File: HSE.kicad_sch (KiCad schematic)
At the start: 5 parts, among them Y1 25MHz

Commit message: BOM cleaned up.
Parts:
- C10, C11: Notes (none) -> or equivalent; Package (none) -> C_0603_1608Metric
- R30: Notes (none) -> or equivalent; Package (none) -> R_0603_1608Metric
- Y1: Notes (none) -> or equivalent; Package (none) -> Crystal_SMD_2016-4Pin_2.0x1.6mm
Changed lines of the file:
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@@
 			)
 		)
-		(property "Datasheet" "~"
+		(property "Datasheet" ""
 			(at 154.94 109.22 0)
 			(effects
@@
 		)
 		(property "MfgPart" "CL10C100JB8NNNC"
+			(at 154.94 109.22 0)
+			(effects
+				(font
+					(size 1.27 1.27)
+				)
+				(hide yes)
+			)
+		)
+		(property "Package" "C_0603_1608Metric"
+			(at 154.94 109.22 0)
+			(effects
+				(font
+					(size 1.27 1.27)
+				)
+				(hide yes)
+			)
+		)
+		(property "Notes" "or equivalent"
 			(at 154.94 109.22 0)
 			(effects
@@
 			)
 		)
-		(property "Datasheet" "~"
+		(property "Datasheet" ""
 			(at 154.94 82.55 0)
 			(effects
@@
 		)
 		(property "MfgPart" "RC0603FR-07634RL"
+			(at 154.94 82.55 0)
+			(effects
+				(font
+					(size 1.27 1.27)
+				)
+				(hide yes)
+			)
+		)
+		(property "Package" "R_0603_1608Metric"
+			(at 154.94 82.55 0)
+			(effects
+				(font
+					(size 1.27 1.27)
+				)
+				(hide yes)
+			)
+		)
+		(property "Notes" "or equivalent"
 			(at 154.94 82.55 0)
 			(effects
@@
 			)
 		)
-		(property "Datasheet" "~"
-			(at 147.32 93.98 0)
-			(effects
-				(font
-					(size 1.27 1.27)
-				)
-				(hide yes)
-			)
-		)
-		(property "Description" "Four pin crystal, GND on pins 2 and 4"
+		(property "Datasheet" "https://support.epson.biz/td/api/doc_check.php?dl=brief_FA-128&lang=en"
+			(at 147.32 93.98 0)
+			(effects
+				(font
+					(size 1.27 1.27)
+				)
+				(hide yes)
+			)
+		)
+		(property "Description" "Four pin crystal, GND on pins 2 and 4, 7pF"
 			(at 147.32 93.98 0)
 			(effects
@@
 		)
 		(property "pads" "4"
+			(at 147.32 93.98 0)
+			(effects
+				(font
+					(size 1.27 1.27)
+				)
+				(hide yes)
+			)
+		)
+		(property "Package" "Crystal_SMD_2016-4Pin_2.0x1.6mm"
+			(at 147.32 93.98 0)
+			(effects
+				(font
+					(size 1.27 1.27)
+				)
+				(hide yes)
+			)
+		)
+		(property "Notes" "or equivalent"
 			(at 147.32 93.98 0)
 			(effects
@@
 			)
 		)
+		(property "Package" ""
+			(at 128.27 123.19 0)
+			(effects
+				(font
+					(size 1.27 1.27)
+				)
+				(hide yes)
+			)
+		)
 		(pin "2"
 		)
@@
 			)
 		)
-		(property "Datasheet" "~"
+		(property "Datasheet" ""
 			(at 138.43 109.22 0)
 			(effects
@@
 			(at 138.43 109.22 0)
 			(effects
+				(font
+					(size 1.27 1.27)
+				)
+				(hide yes)
+			)
+		)
+		(property "Package" "C_0603_1608Metric"
+			(at 138.43 109.22 0)
+			(effects
+				(font
+					(size 1.27 1.27)
+				)
+				(hide yes)
+			)
+		)
+		(property "Notes" "or equivalent"
+			(at 138.43 109.22 0)
+			(effects

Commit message: converted R, C, and L to smaller 0402 footprints. Some trace rearranging and cleanup.
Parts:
- C10, C11: footprint ProjectLib:C_0603_1608Metric -> ProjectLib:C_0402_1005Metric; Manufacturer Samsung -> (none); MfgPart CL10C100JB8NNNC -> (none); Package C_0603_1608Metric -> C_0402_1005Metric
- R30: footprint ProjectLib:R_0603_1608Metric -> ProjectLib:R_0402_1005Metric; Manufacturer Yageo -> (none); MfgPart RC0603FR-07634RL -> (none); Package R_0603_1608Metric -> R_0402_1005Metric
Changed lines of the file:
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@@
 			)
 		)
-		(property "Footprint" "ProjectLib:C_0603_1608Metric"
+		(property "Footprint" "ProjectLib:C_0402_1005Metric"
 			(at 153.9748 105.41 0)
 			(effects
@@
 			)
 		)
-		(property "Manufacturer" "Samsung"
-			(at 154.94 109.22 0)
-			(effects
-				(font
-					(size 1.27 1.27)
-				)
-				(hide yes)
-			)
-		)
-		(property "MfgPart" "CL10C100JB8NNNC"
-			(at 154.94 109.22 0)
-			(effects
-				(font
-					(size 1.27 1.27)
-				)
-				(hide yes)
-			)
-		)
-		(property "Package" "C_0603_1608Metric"
+		(property "Manufacturer" ""
+			(at 154.94 109.22 0)
+			(effects
+				(font
+					(size 1.27 1.27)
+				)
+				(hide yes)
+			)
+		)
+		(property "MfgPart" ""
+			(at 154.94 109.22 0)
+			(effects
+				(font
+					(size 1.27 1.27)
+				)
+				(hide yes)
+			)
+		)
+		(property "Package" "C_0402_1005Metric"
 			(at 154.94 109.22 0)
 			(effects
@@
 			)
 		)
-		(property "Footprint" "ProjectLib:R_0603_1608Metric"
+		(property "Footprint" "ProjectLib:R_0402_1005Metric"
 			(at 155.956 82.804 90)
 			(effects
@@
 			)
 		)
-		(property "Manufacturer" "Yageo"
-			(at 154.94 82.55 0)
-			(effects
-				(font
-					(size 1.27 1.27)
-				)
-				(hide yes)
-			)
-		)
-		(property "MfgPart" "RC0603FR-07634RL"
-			(at 154.94 82.55 0)
-			(effects
-				(font
-					(size 1.27 1.27)
-				)
-				(hide yes)
-			)
-		)
-		(property "Package" "R_0603_1608Metric"
+		(property "Manufacturer" ""
+			(at 154.94 82.55 0)
+			(effects
+				(font
+					(size 1.27 1.27)
+				)
+				(hide yes)
+			)
+		)
+		(property "MfgPart" ""
+			(at 154.94 82.55 0)
+			(effects
+				(font
+					(size 1.27 1.27)
+				)
+				(hide yes)
+			)
+		)
+		(property "Package" "R_0402_1005Metric"
 			(at 154.94 82.55 0)
 			(effects
@@
 			)
 		)
-		(property "Footprint" "ProjectLib:C_0603_1608Metric"
+		(property "Footprint" "ProjectLib:C_0402_1005Metric"
 			(at 137.4648 105.41 0)
 			(effects
@@
 			)
 		)
-		(property "Manufacturer" "Samsung"
+		(property "Manufacturer" ""
 			(at 138.43 109.22 0)
 			(effects
@@
 			)
 		)
-		(property "MfgPart" "CL10C100JB8NNNC"
+		(property "MfgPart" ""
 			(at 138.43 109.22 0)
 			(effects
@@
 			)
 		)
-		(property "Package" "C_0603_1608Metric"
+		(property "Package" "C_0402_1005Metric"
 			(at 138.43 109.22 0)
 			(effects

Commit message: improved schematic sheet titles.
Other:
- title: ADCs for 10K thermistors -> HSE
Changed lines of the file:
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@@
 	(paper "A4")
 	(title_block
-		(title "ADCs for 10K thermistors")
-		(date "2025-01-07")
-		(rev "v0.1.1")
+		(title "HSE")
+		(date "2025-09-15")
+		(rev "v0.2.2")
 	)
 	(junction

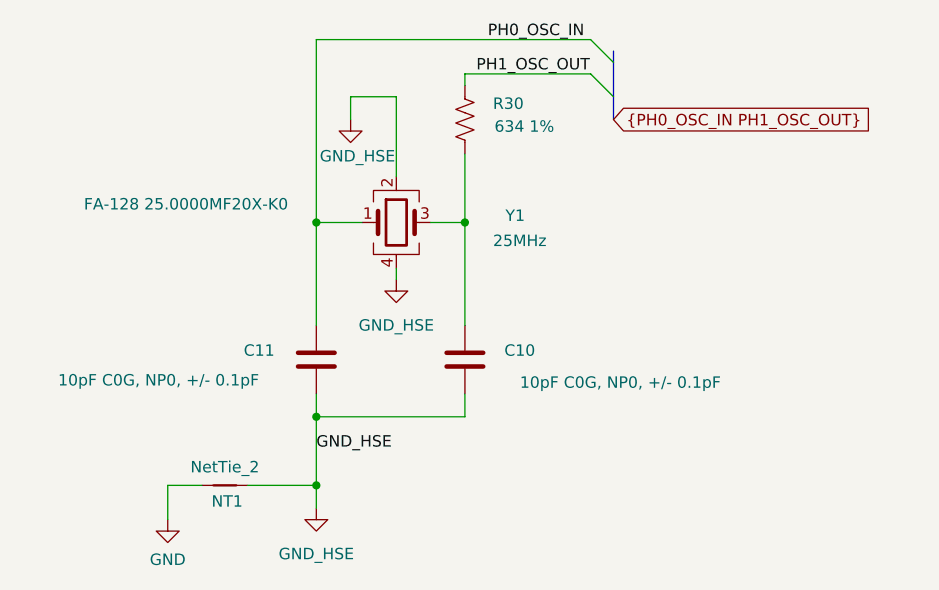
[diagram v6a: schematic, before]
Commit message: added QR and ID blocks on silkscreen. Marked HSE and LSE as DNP. Revised version number to 0.3.1.
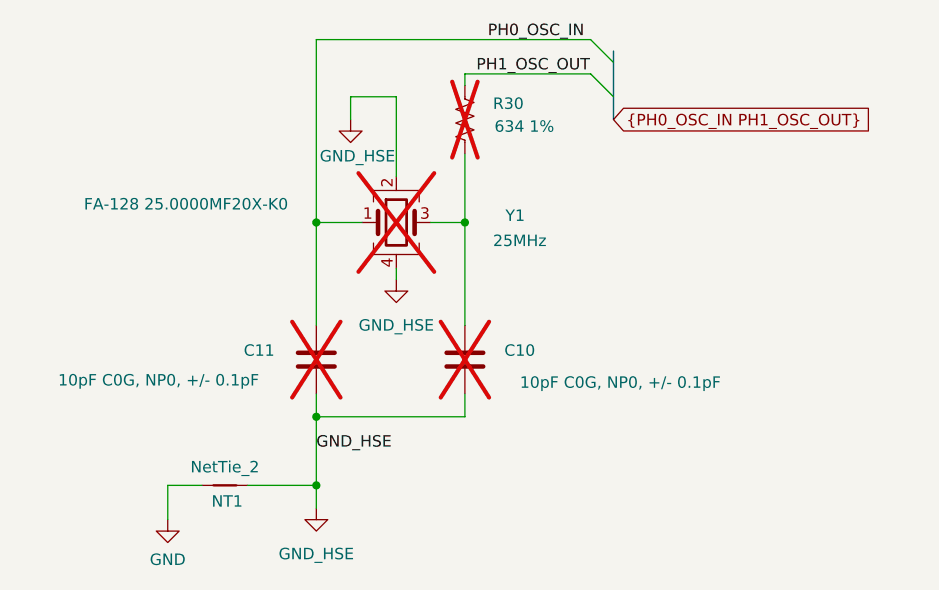
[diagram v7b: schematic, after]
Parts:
- C10, C11, R30, Y1: now not fitted
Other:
- title: HSE -> stm32f411, RFM95W
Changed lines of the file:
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@@
 	(paper "A4")
 	(title_block
-		(title "HSE")
-		(date "2025-09-15")
-		(rev "v0.2.2")
+		(title "stm32f411, RFM95W")
+		(date "2026-04-12")
+		(rev "v0.3.1")
 	)
 	(junction
@@
 		(in_bom yes)
 		(on_board yes)
-		(in_pos_files yes)
-		(dnp no)
+		(in_pos_files no)
+		(dnp yes)
 		(property "Reference" "C10"
 			(at 161.036 108.204 0)
@@
 		(in_bom yes)
 		(on_board yes)
-		(in_pos_files yes)
-		(dnp no)
+		(in_pos_files no)
+		(dnp yes)
 		(property "Reference" "R30"
 			(at 159.766 80.772 0)
@@
 		(in_bom yes)
 		(on_board yes)
-		(in_pos_files yes)
-		(dnp no)
+		(in_pos_files no)
+		(dnp yes)
 		(property "Reference" "Y1"
 			(at 160.528 93.218 0)
@@
 		(in_bom yes)
 		(on_board yes)
-		(in_pos_files yes)
-		(dnp no)
+		(in_pos_files no)
+		(dnp yes)
 		(property "Reference" "C11"
 			(at 132.08 108.204 0)
